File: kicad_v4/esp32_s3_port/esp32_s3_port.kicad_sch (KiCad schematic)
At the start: 50 parts, among them J1 Battery, J2 PINHD_1x2_Female, J3 misc Pogo pin connector, SW1 KS33_SW_HS, SW10 KS33_SW_HS, SW11 KS33_SW_HS, SW12 KS33_SW_HS, SW13 KS33_SW_HS, SW14 KS33_SW_HS, SW15 KS33_SW_HS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

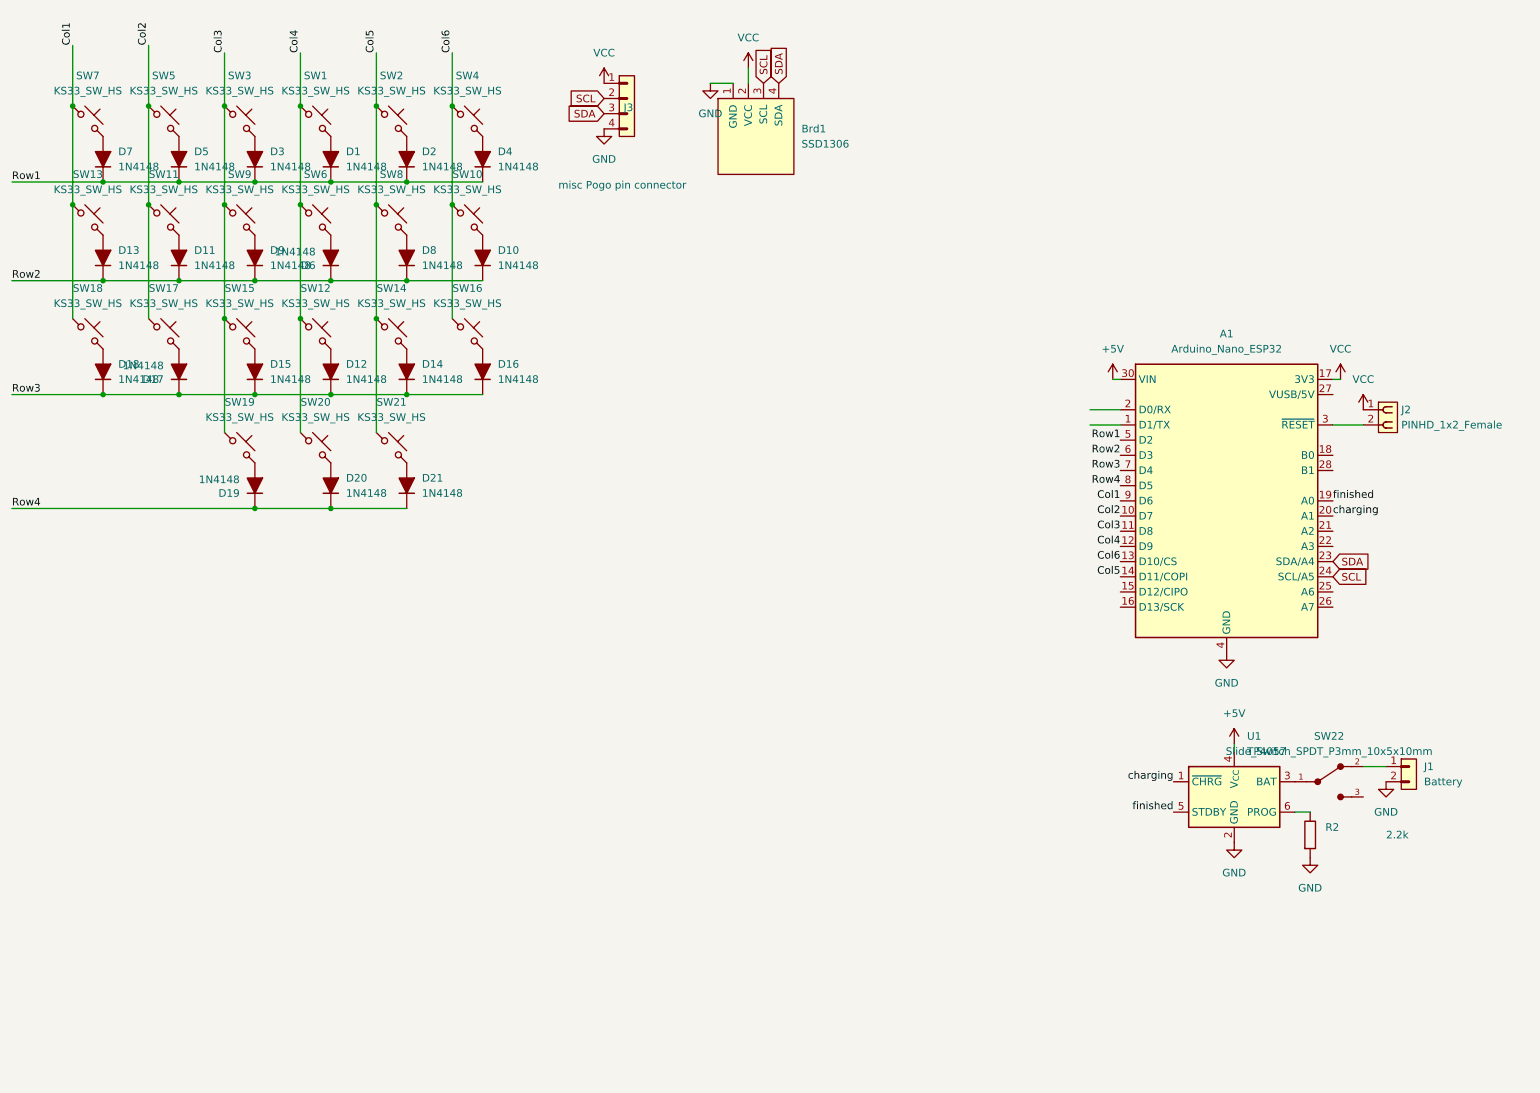
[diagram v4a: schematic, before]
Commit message: surface mount version
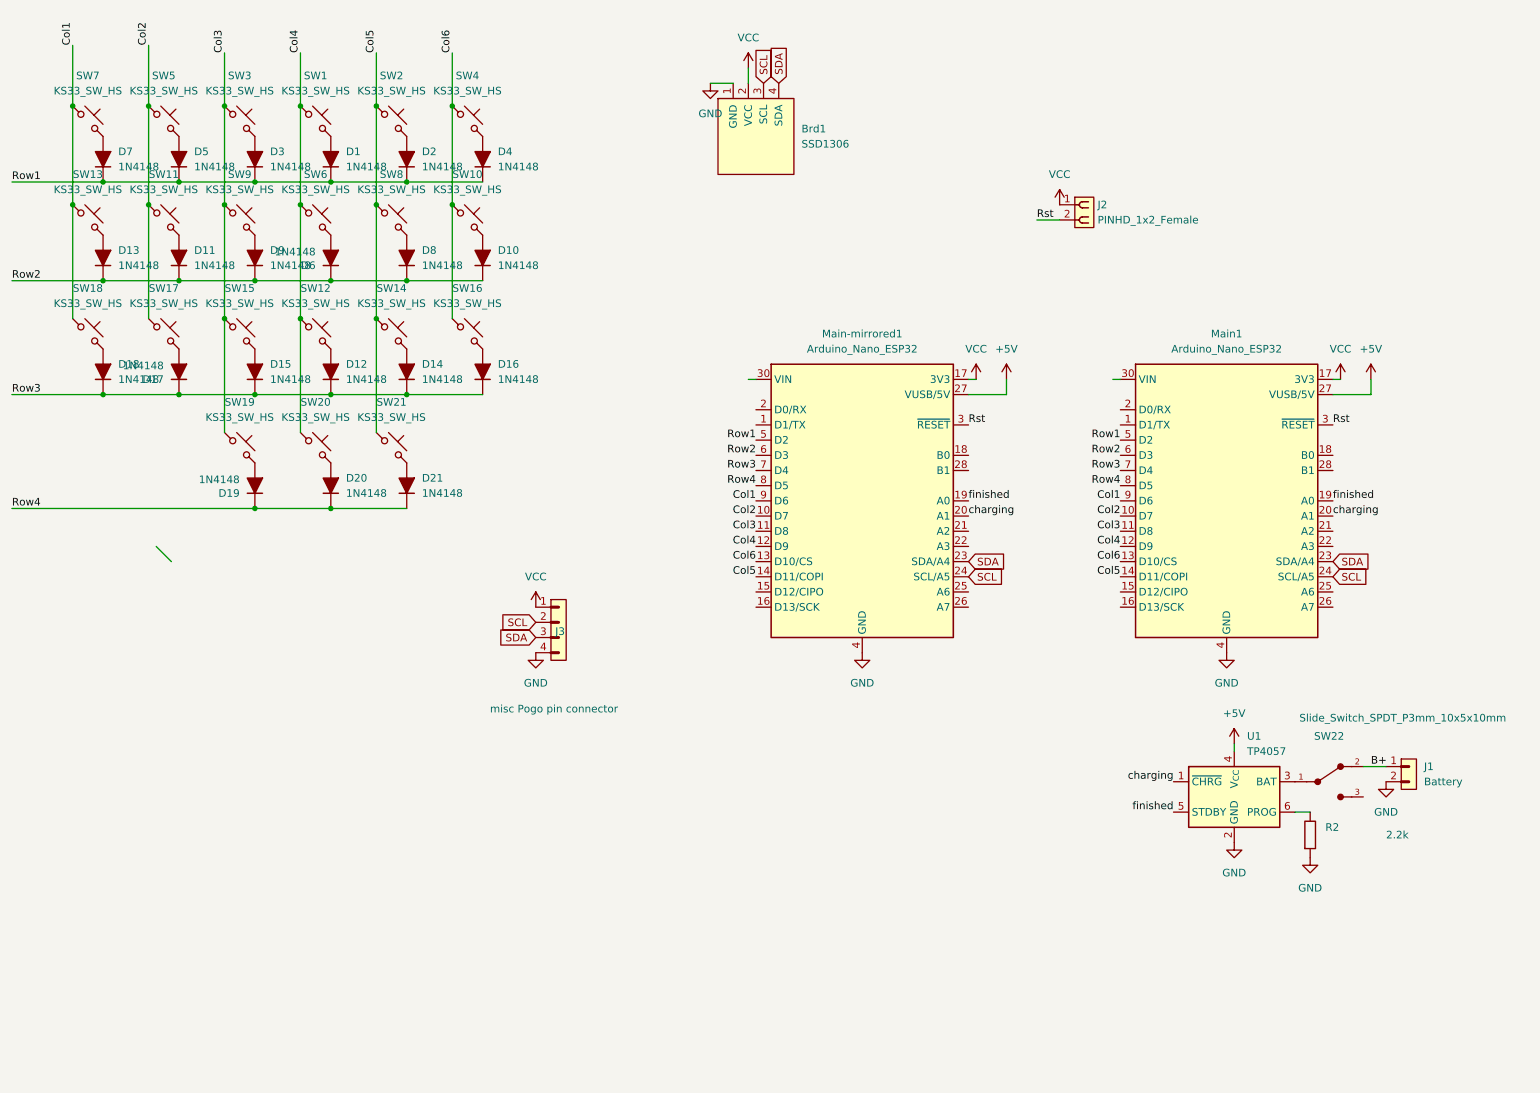
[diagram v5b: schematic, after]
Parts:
- added Main-mirrored1: Arduino_Nano_ESP32, Module:Arduino_Nano, symbol MCU_Module:Arduino_Nano_ESP32
- renumbered A1 to Main1
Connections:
- net +5V: now also Main1.27 (VUSB/5V), Main-mirrored1.27 (VUSB/5V); no longer Main1.30 (VIN)
- net Col1: now also Main-mirrored1.9 (D6)
- net Col2: now also Main-mirrored1.10 (D7)
- net Col3: now also Main-mirrored1.11 (D8)
- net Col4: now also Main-mirrored1.12 (D9)
- net Col5: now also Main-mirrored1.14 (D11/COPI)
- net Col6: now also Main-mirrored1.13 (D10/CS)
- net GND: now also Main-mirrored1.29 (GND), Main-mirrored1.4 (GND)
- net Row1: now also Main-mirrored1.5 (D2)
- net Row2: now also Main-mirrored1.6 (D3)
- net Row3: now also Main-mirrored1.7 (D4)
- net Row4: now also Main-mirrored1.8 (D5)
- net SCL: now also Main-mirrored1.24 (SCL/A5)
- net SDA: now also Main-mirrored1.23 (SDA/A4)
- net VCC: now also Main-mirrored1.17 (3V3)
- net charging: now also Main-mirrored1.20 (A1)
- net finished: now also Main-mirrored1.19 (A0)
- net Rst: now reaches J2.2, Main1.3 (~{RESET})
- net Rst: now also Main-mirrored1.3 (~{RESET})
- net B+: now reaches J1.1, SW22.2
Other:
- moved on the sheet: J2, J3
